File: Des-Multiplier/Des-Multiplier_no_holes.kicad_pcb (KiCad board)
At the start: 2 copper layers, 100 x 100 mm, 61 parts, among them U1 NE555P, U10 74HC00, U11 74HC00, U12 74LS194, U13 74HC00, U14 74HC00, U2 NE555P, U3 74LS194, U4 74LS283, U5 74LS273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

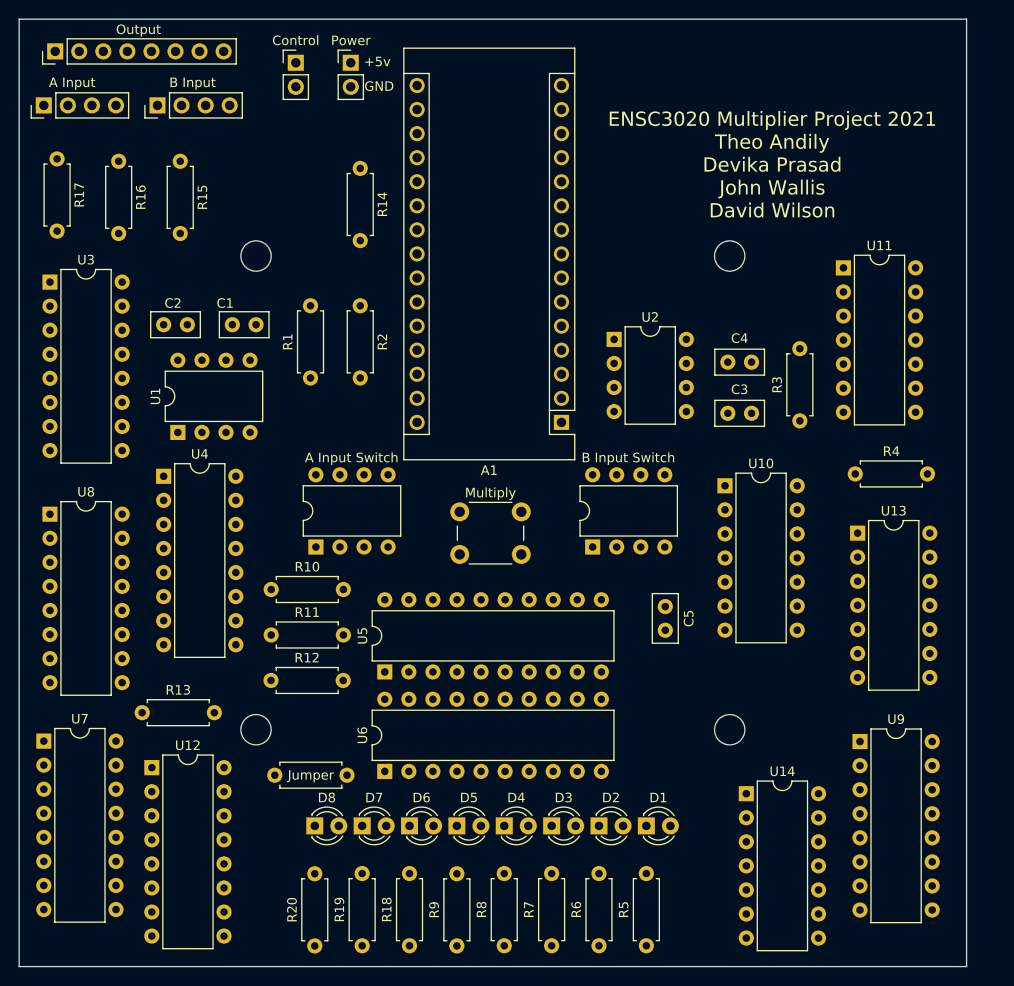
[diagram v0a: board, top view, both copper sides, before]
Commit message: mounting hole respins
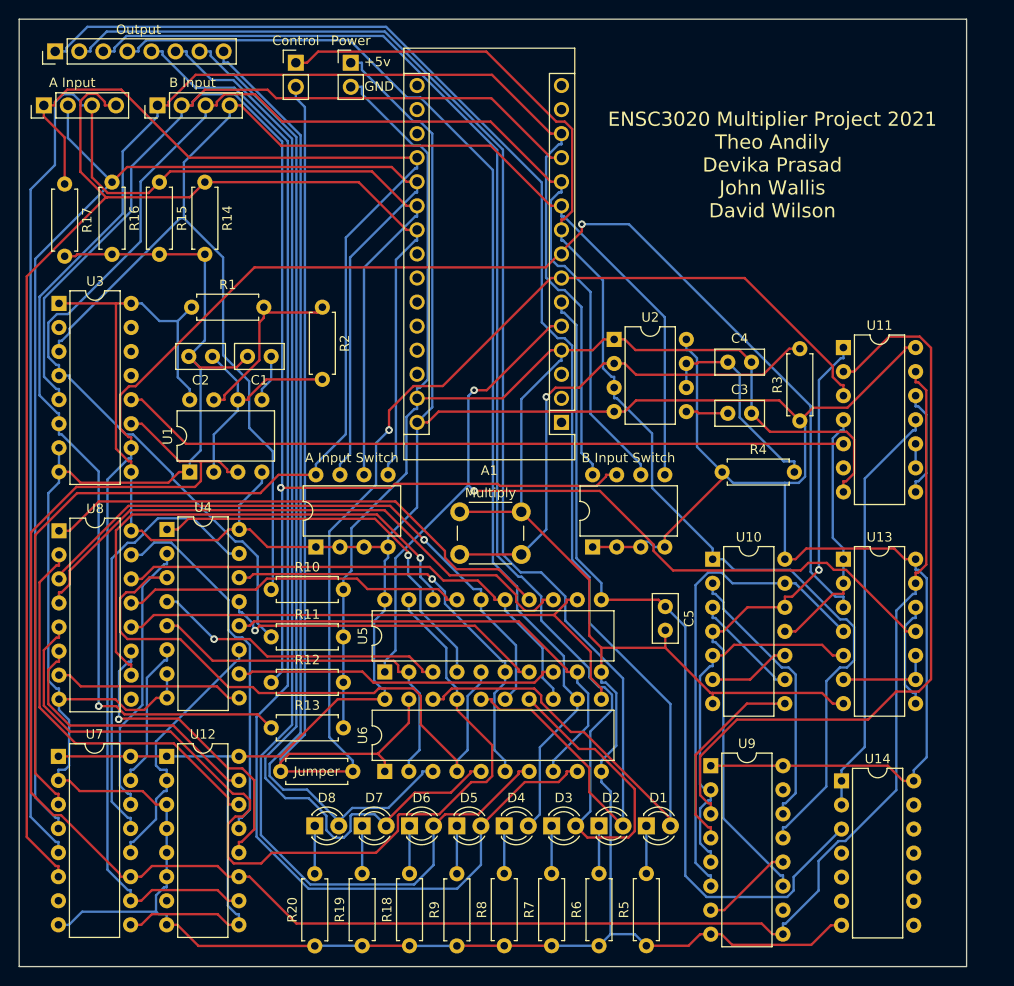
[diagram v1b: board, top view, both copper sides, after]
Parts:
- removed REF1, REF2, REF3, REF4: MountingHole_3.2mm_M3, MountingHole:MountingHole_3.2mm_M3
- moved R14 16.5 mm to (119.6, 70.2)
- moved U9 16.0 mm to (173.0, 131.8)
- moved R1 14.6 mm to (118.2, 83.4), turned to 0 degrees
- moved R4 14.1 mm to (174.2, 100.8)
- moved R13 13.7 mm to (126.6, 127.8)
- moved U14 10.1 mm to (186.8, 133.4)
- moved U11 8.41 mm to (187.0, 87.7)
- moved U10 7.86 mm to (173.2, 110.0)
- moved U4 5.62 mm to (115.6, 106.9)
- moved U1 4.36 mm to (118.0, 100.8)
- moved C2 4.27 mm to (120.4, 88.6)
- moved R2 4.00 mm to (132.0, 83.4)
- moved C1 3.71 mm to (126.6, 88.6)
- moved U13 3.13 mm to (187.0, 110.0)
- moved R15 3.11 mm to (114.8, 70.2)
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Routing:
- net GND: track 0.00 -> 471.6 mm
- net +5V: track 0.00 -> 405.1 mm
- net /CLK: track 0.00 -> 217.1 mm
- net /A1: track 0.00 -> 189.2 mm, vias 0 -> 1
- net /~Ashift~\Load: track 0.00 -> 180.9 mm, vias 0 -> 1
- net /A0: track 0.00 -> 176.6 mm, vias 0 -> 1
- net /Out0: track 0.00 -> 166.0 mm
- net /B2: track 0.00 -> 162.5 mm
- net /B3: track 0.00 -> 155.8 mm
- net /A2: track 0.00 -> 153.1 mm
- net /Out2: track 0.00 -> 152.5 mm
- net /B0: track 0.00 -> 152.4 mm
- net /Out1: track 0.00 -> 151.1 mm
- net /B1: track 0.00 -> 150.7 mm
- net /A3: track 0.00 -> 149.5 mm
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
